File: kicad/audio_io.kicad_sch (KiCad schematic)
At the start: 16 parts, among them J3 AudioJack3_Switch, J4 AudioJack3_Switch, J8 NMJ4HCD2, J9 NMJ4HCD2, SW6 SW_Slide_DPDT, U5 OPA1678

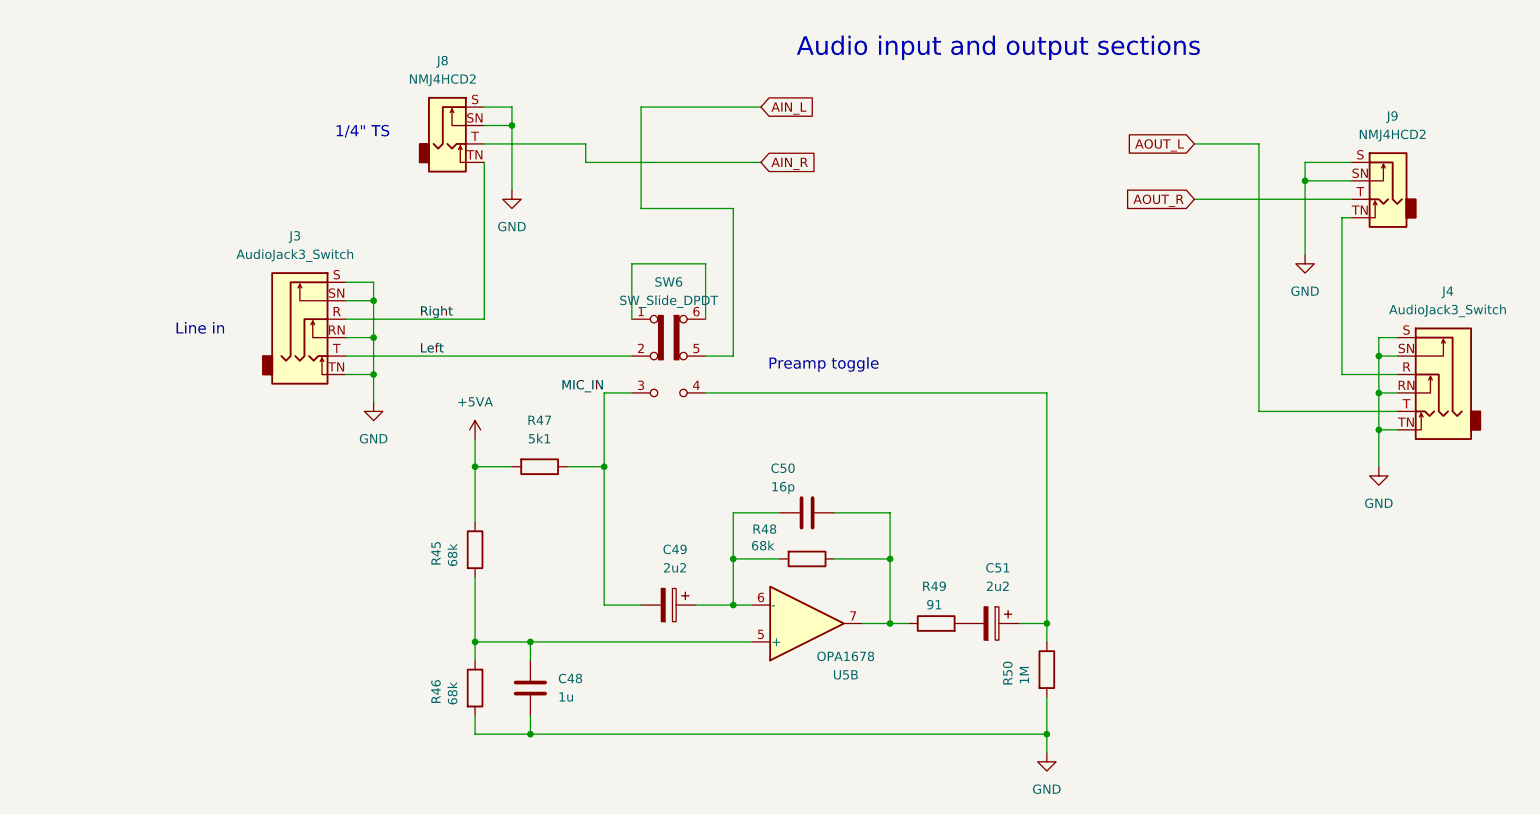
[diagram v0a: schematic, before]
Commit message: started with PCB layout. Might want to move I2S
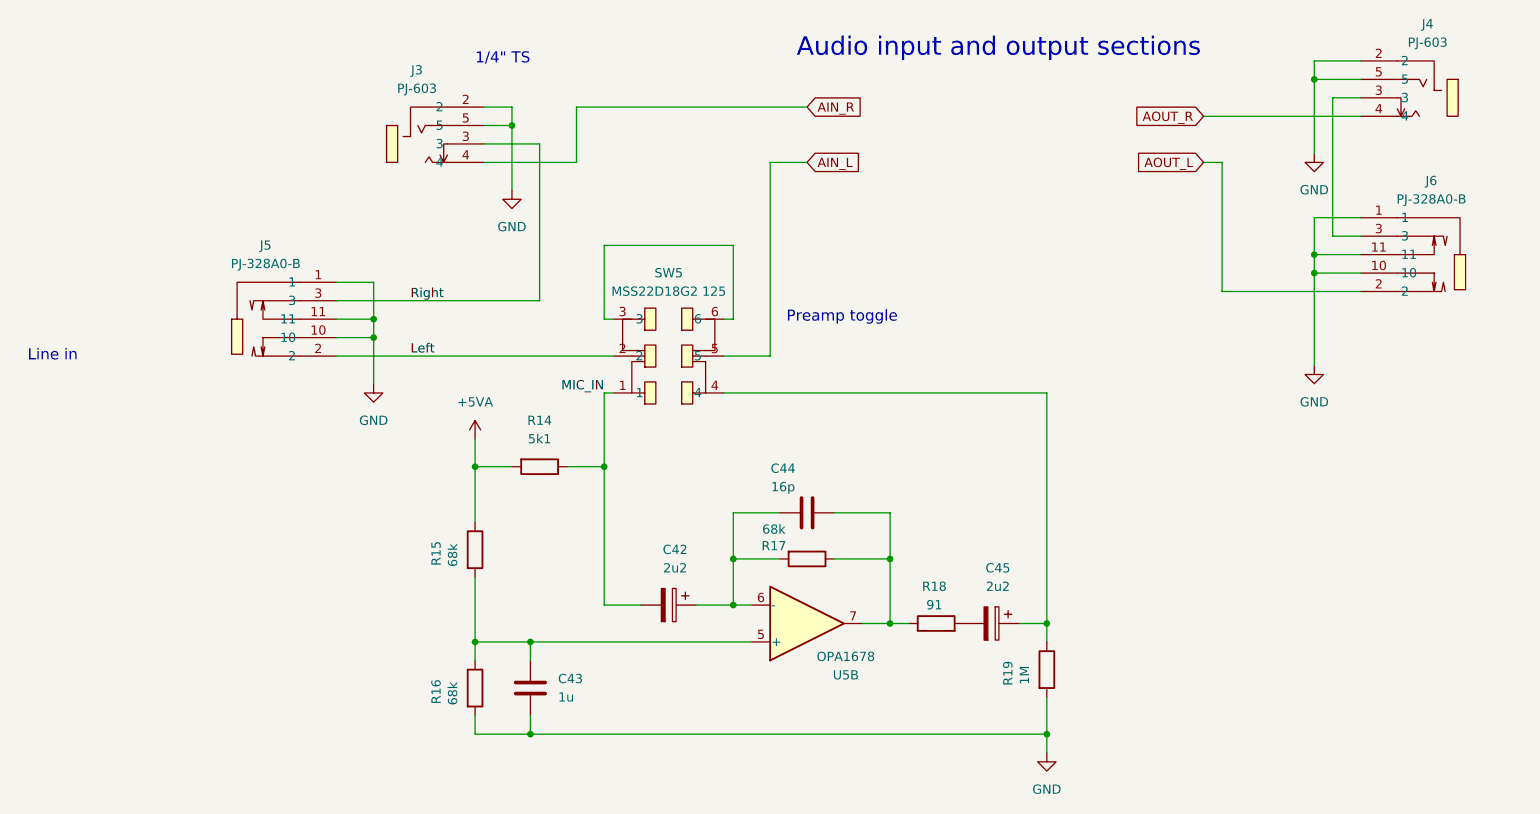
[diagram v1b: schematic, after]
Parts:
- removed J3, J4: AudioJack3_Switch, symbol Connector_Audio:AudioJack3_Switch
- removed J8, J9: NMJ4HCD2, Connector_Audio:Jack_6.35mm_Neutrik_NMJ4HCD2_Horizontal, symbol Connector_Audio:NMJ4HCD2
- removed R48: 68k, symbol Device:R
- removed SW6: SW_Slide_DPDT, symbol Switch:SW_Slide_DPDT
- added J3, J4: PJ-603, easyeda2kicad:AUDIO-TH_PJ-603, symbol easyeda2kicad:PJ-603
- added J5, J6: PJ-328A0-B, easyeda2kicad:AUDIO-TH_PJ-328A0-B, symbol easyeda2kicad:PJ-328A0-B
- added R17: 68k, Resistor_SMD:R_0402_1005Metric, symbol Device:R
- added SW5: MSS22D18G2 125, easyeda2kicad:SW-TH_SHOU_MSS22D18G2, symbol easyeda2kicad:MSS22D18G2125
- C42: renamed from C49; footprint (none) -> Capacitor_SMD:CP_Elec_4x5.4
- C43: renamed from C48; footprint (none) -> Capacitor_SMD:C_0402_1005Metric
- C44: renamed from C50; footprint (none) -> Capacitor_SMD:C_0402_1005Metric
- C45: renamed from C51; footprint (none) -> Capacitor_SMD:CP_Elec_4x5.4
- R14: renamed from R47; footprint (none) -> Resistor_SMD:R_0402_1005Metric
- R15: renamed from R45; footprint (none) -> Resistor_SMD:R_0402_1005Metric
- R16: renamed from R46; footprint (none) -> Resistor_SMD:R_0402_1005Metric
- R18: renamed from R49; footprint (none) -> Resistor_SMD:R_0402_1005Metric
- R19: renamed from R50; footprint (none) -> Resistor_SMD:R_0402_1005Metric
- U5: footprint (none) -> Package_SO:SOIC-8_3.9x4.9mm_P1.27mm
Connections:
- net AIN_L: now also SW5.5
- net AIN_R: now also J3.4
- net AOUT_L: now also J6.2
- net AOUT_R: now also J4.4
- net GND: now also J3.2, J3.5, J4.2, J4.5, J5.1, J5.10, J5.11, J6.1, J6.10, J6.11
- net Left: now also J5.2, SW5.2
- net MIC_IN: now also SW5.1
- net Right: now also J3.3, J5.3
- net at C42.1, C44.1, U5.6 (-): now also R17.2
- net at C45.1, R19.1: now also SW5.4
- net at C44.2, R18.1, U5.7: now also R17.1
- new net: SW5.3, SW5.6
- new net: J4.3, J6.3

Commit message: aaaa
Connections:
- net MIC_IN: now also SW5.3; no longer SW5.1
- net at SW5.6: now also C45.1, R19.1; no longer SW5.3
- new net: SW5.1, SW5.4
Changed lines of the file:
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@@
 	(text "Preamp toggle"
 		(exclude_from_sim no)
-		(at 136.906 92.456 0)
+		(at 134.874 95.25 0)
 		(effects
 			(font
@@
 	)
 	(junction
+		(at 165.1 149.86)
+		(diameter 0)
+		(color 0 0 0 0)
+	)
+	(junction
+		(at 201.93 59.69)
+		(diameter 0)
+		(color 0 0 0 0)
+	)
+	(junction
+		(at 91.44 66.04)
+		(diameter 0)
+		(color 0 0 0 0)
+	)
+	(junction
+		(at 86.36 137.16)
+		(diameter 0)
+		(color 0 0 0 0)
+	)
+	(junction
+		(at 72.39 92.71)
+		(diameter 0)
+		(color 0 0 0 0)
+	)
+	(junction
+		(at 143.51 125.73)
+		(diameter 0)
+		(color 0 0 0 0)
+	)
+	(junction
+		(at 86.36 113.03)
+		(diameter 0)
+		(color 0 0 0 0)
+	)
+	(junction
+		(at 121.92 132.08)
+		(diameter 0)
+		(color 0 0 0 0)
+	)
+	(junction
+		(at 201.93 86.36)
+		(diameter 0)
+		(color 0 0 0 0)
+	)
+	(junction
+		(at 93.98 137.16)
+		(diameter 0)
+		(color 0 0 0 0)
+	)
+	(junction
+		(at 93.98 149.86)
+		(diameter 0)
+		(color 0 0 0 0)
+	)
+	(junction
+		(at 72.39 95.25)
+		(diameter 0)
+		(color 0 0 0 0)
+	)
+	(junction
+		(at 121.92 125.73)
+		(diameter 0)
+		(color 0 0 0 0)
+	)
+	(junction
+		(at 143.51 134.62)
+		(diameter 0)
+		(color 0 0 0 0)
+	)
+	(junction
 		(at 104.14 113.03)
 		(diameter 0)
@@
 	)
 	(junction
-		(at 165.1 149.86)
-		(diameter 0)
-		(color 0 0 0 0)
-	)
-	(junction
-		(at 201.93 59.69)
-		(diameter 0)
-		(color 0 0 0 0)
-	)
-	(junction
-		(at 91.44 66.04)
-		(diameter 0)
-		(color 0 0 0 0)
-	)
-	(junction
-		(at 86.36 137.16)
-		(diameter 0)
-		(color 0 0 0 0)
-	)
-	(junction
-		(at 72.39 92.71)
-		(diameter 0)
-		(color 0 0 0 0)
-	)
-	(junction
-		(at 143.51 125.73)
-		(diameter 0)
-		(color 0 0 0 0)
-	)
-	(junction
-		(at 86.36 113.03)
-		(diameter 0)
-		(color 0 0 0 0)
-	)
-	(junction
-		(at 121.92 132.08)
-		(diameter 0)
-		(color 0 0 0 0)
-	)
-	(junction
-		(at 201.93 86.36)
-		(diameter 0)
-		(color 0 0 0 0)
-	)
-	(junction
-		(at 93.98 137.16)
-		(diameter 0)
-		(color 0 0 0 0)
-	)
-	(junction
-		(at 93.98 149.86)
-		(diameter 0)
-		(color 0 0 0 0)
-	)
-	(junction
-		(at 72.39 95.25)
-		(diameter 0)
-		(color 0 0 0 0)
-	)
-	(junction
-		(at 121.92 125.73)
-		(diameter 0)
-		(color 0 0 0 0)
-	)
-	(junction
-		(at 143.51 134.62)
-		(diameter 0)
-		(color 0 0 0 0)
-	)
-	(junction
 		(at 201.93 83.82)
 		(diameter 0)
@@
 	(wire
 		(pts
-			(xy 104.14 92.71) (xy 104.14 82.55)
-		)
-		(stroke
-			(width 0)
-			(type default)
-		)
-	)
-	(wire
-		(pts
 			(xy 135.89 125.73) (xy 143.51 125.73)
 		)
@@
 	(wire
 		(pts
+			(xy 105.41 106.68) (xy 120.65 106.68)
+		)
+		(stroke
+			(width 0)
+			(type default)
+		)
+	)
+	(wire
+		(pts
 			(xy 67.31 95.25) (xy 72.39 95.25)
 		)
@@
 	(wire
 		(pts
-			(xy 127 71.12) (xy 127 97.79)
-		)
-		(stroke
-			(width 0)
-			(type default)
-		)
-	)
-	(wire
-		(pts
 			(xy 87.63 71.12) (xy 100.33 71.12)
 		)
@@
 	(wire
 		(pts
+			(xy 67.31 97.79) (xy 105.41 97.79)
+		)
+		(stroke
+			(width 0)
+			(type default)
+		)
+	)
+	(wire
+		(pts
 			(xy 86.36 137.16) (xy 93.98 137.16)
 		)
@@
 	(wire
 		(pts
+			(xy 120.65 97.79) (xy 125.73 97.79)
+		)
+		(stroke
+			(width 0)
+			(type default)
+		)
+	)
+	(wire
+		(pts
 			(xy 128.27 119.38) (xy 121.92 119.38)
 		)
@@
 	(wire
 		(pts
+			(xy 104.14 92.71) (xy 104.14 113.03)
+		)
+		(stroke
+			(width 0)
+			(type default)
+		)
+	)
+	(wire
+		(pts
 			(xy 208.28 78.74) (xy 201.93 78.74)
 		)
@@
 	(wire
 		(pts
-			(xy 104.14 102.87) (xy 104.14 113.03)
-		)
-		(stroke
-			(width 0)
-			(type default)
-		)
-	)
-	(wire
-		(pts
 			(xy 121.92 119.38) (xy 121.92 125.73)
 		)
@@
 	(wire
 		(pts
-			(xy 67.31 97.79) (xy 105.41 97.79)
-		)
-		(stroke
-			(width 0)
-			(type default)
-		)
-	)
-	(wire
-		(pts
-			(xy 165.1 102.87) (xy 165.1 134.62)
-		)
-		(stroke
-			(width 0)
-			(type default)
-		)
-	)
-	(wire
-		(pts
 			(xy 201.93 59.69) (xy 208.28 59.69)
 		)
@@
 	(wire
 		(pts
-			(xy 104.14 102.87) (xy 105.41 102.87)
-		)
-		(stroke
-			(width 0)
-			(type default)
-		)
-	)
-	(wire
-		(pts
 			(xy 87.63 63.5) (xy 91.44 63.5)
 		)
@@
 	(wire
 		(pts
+			(xy 165.1 92.71) (xy 165.1 134.62)
+		)
+		(stroke
+			(width 0)
+			(type default)
+		)
+	)
+	(wire
+		(pts
 			(xy 109.22 132.08) (xy 104.14 132.08)
 		)
@@
 	(wire
 		(pts
-			(xy 127 71.12) (xy 132.08 71.12)
-		)
-		(stroke
-			(width 0)
-			(type default)
-		)
-	)
-	(wire
-		(pts
 			(xy 93.98 149.86) (xy 165.1 149.86)
 		)
@@
 	(wire
 		(pts
-			(xy 121.92 92.71) (xy 121.92 82.55)
-		)
-		(stroke
-			(width 0)
-			(type default)
-		)
-	)
-	(wire
-		(pts
 			(xy 95.25 68.58) (xy 87.63 68.58)
 		)
@@
 	(wire
 		(pts
+			(xy 120.65 106.68) (xy 120.65 102.87)
+		)
+		(stroke
+			(width 0)
+			(type default)
+		)
+	)
+	(wire
+		(pts
 			(xy 95.25 68.58) (xy 95.25 90.17)
 		)
@@
 	(wire
 		(pts
-			(xy 120.65 102.87) (xy 165.1 102.87)
+			(xy 125.73 71.12) (xy 132.08 71.12)
 		)
 		(stroke
@@
 	(wire
 		(pts
-			(xy 104.14 82.55) (xy 121.92 82.55)
+			(xy 125.73 97.79) (xy 125.73 71.12)
 		)
 		(stroke
@@
 	(wire
 		(pts
-			(xy 120.65 92.71) (xy 121.92 92.71)
-		)
-		(stroke
-			(width 0)
-			(type default)
-		)
-	)
-	(wire
-		(pts
-			(xy 120.65 97.79) (xy 127 97.79)
-		)
-		(stroke
+			(xy 120.65 92.71) (xy 165.1 92.71)
+		)
+		(stroke
+			(width 0)
+			(type default)
+		)
+	)
+	(wire
+		(pts
+			(xy 105.41 102.87) (xy 105.41 106.68)
+		)
+		(stroke

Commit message: aaa
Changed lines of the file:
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@@
 	(text "Line in"
 		(exclude_from_sim no)
-		(at 28.194 97.79 0)
+		(at 61.214 101.6 0)
 		(effects
 			(font
